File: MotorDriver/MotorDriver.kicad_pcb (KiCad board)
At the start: 2 copper layers, 109.9 x 40.6 mm, 66 parts, among them J1 Phase A, J10 PWR_D, J11 USART, J2 Phase B, J3 Phase C, J4 CAN, J5 IdSelect, J6 ST_LINK, J7 Hall, J8 Vbat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

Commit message: Finished printable parts
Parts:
- added C20: 10n, Capacitor_SMD:C_0603_1608Metric_Pad1.05x0.95mm_HandSolder, B.Cu at (134.6, 106.1)
- added C21: 10n, Capacitor_SMD:C_0603_1608Metric_Pad1.05x0.95mm_HandSolder, B.Cu at (134.6, 104.5)
- added C22: 10n, Capacitor_SMD:C_0603_1608Metric_Pad1.05x0.95mm_HandSolder, B.Cu at (134.6, 103.1)
- added C23: 100n, Capacitor_SMD:C_0603_1608Metric_Pad1.05x0.95mm_HandSolder, F.Cu at (133.1, 110.3)
- added D5: MRA4003T3G, Diode_SMD:D_SMA-SMB_Universal_Handsoldering, B.Cu at (125.9, 111.5)
- added R19: 100, Resistor_SMD:R_0603_1608Metric_Pad1.05x0.95mm_HandSolder, F.Cu at (131.9, 89.0)
- added R20: 100, Resistor_SMD:R_0603_1608Metric_Pad1.05x0.95mm_HandSolder, F.Cu at (131.9, 87.2)
- added R21: 3k3, Resistor_SMD:R_0603_1608Metric_Pad1.05x0.95mm_HandSolder, F.Cu at (138.2, 106.8)
- added R22: 3k3, Resistor_SMD:R_0603_1608Metric_Pad1.05x0.95mm_HandSolder, F.Cu at (140.7, 106.8)
- added R23: 3k3, Resistor_SMD:R_0603_1608Metric_Pad1.05x0.95mm_HandSolder, F.Cu at (143.3, 106.8)
- added R24: 2k2, Resistor_SMD:R_0603_1608Metric_Pad1.05x0.95mm_HandSolder, B.Cu at (138.2, 106.8)
- added R25: 2k2, Resistor_SMD:R_0603_1608Metric_Pad1.05x0.95mm_HandSolder, B.Cu at (140.7, 106.8)
- added R26: 2k2, Resistor_SMD:R_0603_1608Metric_Pad1.05x0.95mm_HandSolder, B.Cu at (143.3, 106.8)
- C16: moved to B.Cu
- D1: footprint Diode_SMD:D_SMA -> Diode_SMD:D_SMA-SMB_Universal_Handsoldering; moved to B.Cu
- moved D3 24.4 mm to (126.2, 107.4)
- moved C10 23.4 mm to (128.1, 108.5)
- moved C5 23.1 mm to (130.0, 108.5)
- moved R3 23.0 mm to (131.6, 108.5)
- moved D1 22.7 mm to (108.3, 107.5), turned to 90 degrees
- moved R14 22.7 mm to (121.7, 108.1)
- moved C16 21.7 mm to (134.6, 101.5)
- moved J2 21.3 mm to (196.1, 94.2)
- moved J5 21.3 mm to (137.0, 94.6)
- moved Q3 21.3 mm to (182.0, 94.2)
- moved C1 21.3 mm to (108.5, 102.6)
- moved H1 21.3 mm to (202.4, 109.5)
- moved H2 21.3 mm to (202.4, 79.0)
- moved J1 21.3 mm to (196.1, 103.8)
- moved J3 21.3 mm to (196.1, 84.7)
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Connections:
- J11 pad 2: /procesorová jednotka/USART_TX -> Net-(J11-Pad2)
- J11 pad 3: /procesorová jednotka/USART_RX -> Net-(J11-Pad3)
- J7 pad 2: /procesorová jednotka/HAL_C -> Net-(J7-Pad2)
- J7 pad 3: /procesorová jednotka/HAL_B -> Net-(J7-Pad3)
- J7 pad 4: /procesorová jednotka/HAL_A -> Net-(J7-Pad4)
- J7 pad 5: +5V -> Net-(C23-Pad1)
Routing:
- net GNDS: track 220.7 -> 163.1 mm, vias 20 -> 19
- net +3V3: track 82.9 -> 106.8 mm, vias 5 -> 7
- net +5V: track 55.3 -> 41.3 mm, vias 0 -> 1
- net Net-(J11-Pad2): track 0.00 -> 12.2 mm
- net /procesorová jednotka/USART_TX: track 16.0 -> 5.02 mm
- net +9V: track 15.6 -> 8.99 mm
- net Net-(C23-Pad1): track 0.00 -> 6.50 mm, vias 0 -> 1
- net Net-(J11-Pad3): track 0.00 -> 5.64 mm
- net Net-(J7-Pad4): track 0.00 -> 5.08 mm
- net Net-(J7-Pad3): track 0.00 -> 5.08 mm
- net Net-(J7-Pad2): track 0.00 -> 5.08 mm
- net /procesorová jednotka/USART_RX: track 11.8 -> 7.29 mm
- net /power/pwrs_in: track 6.23 -> 9.10 mm, vias 0 -> 1
- net /procesorová jednotka/HAL_A: track 23.3 -> 21.7 mm, vias 0 -> 1
- net /procesorová jednotka/CONF_2: track 12.3 -> 13.7 mm
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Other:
- net class PWR: clearance 0.5 -> 0.2
- net class PWRS: clearance 0.3 -> 0.2
- net class PWRS_IN: clearance 0.3 -> 0.2
- board text added: "A"
- board text added: "B"
- board text added: "C"
- board text added: "Hall"
- board text added: "Murphy II Motor driver rev. 1.0"
- board text added: "PhA"
- board text added: "PhB"
- board text added: "PhC"
- board text removed: "HA"
- board text removed: "HB"
- board text removed: "HC"

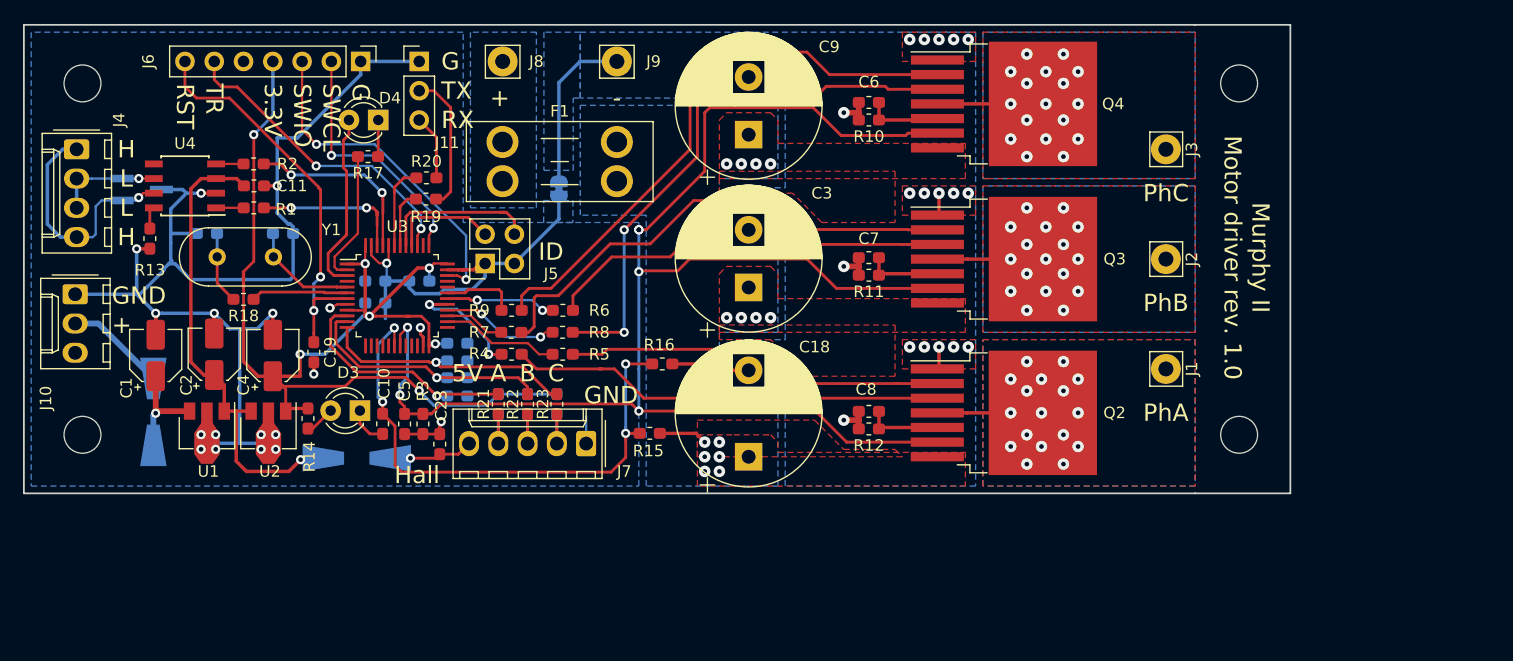
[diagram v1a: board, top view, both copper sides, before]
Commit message: Power and output ping changed roblaced by holes. Correction of tracks width and vias diameters.
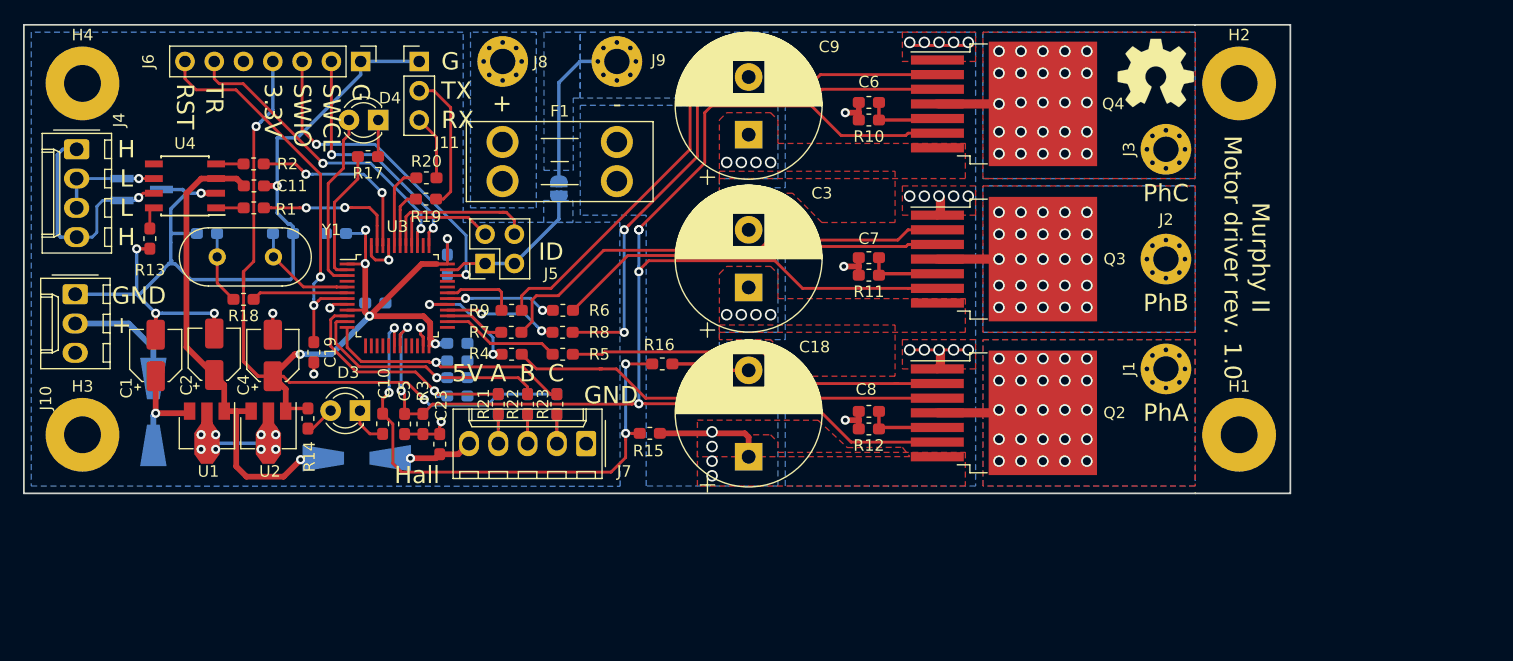
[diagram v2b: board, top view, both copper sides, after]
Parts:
- added REF**: OSHW-Symbol_6.7x6mm_SilkScreen, Symbol:OSHW-Symbol_6.7x6mm_SilkScreen, F.Cu at (195.2, 78.1)
- H1, H2, H3, H4: value MountingHole -> MountingHole_Pad; footprint MountingHole:MountingHole_3.2mm_M3_ISO7380 -> MountingHole:MountingHole_3.2mm_M3_Pad
- J1, J2, J3, J9: footprint Connector_Pin:Pin_D1.4mm_L8.5mm_W2.8mm_FlatFork -> MountingHole:MountingHole_2.2mm_M2_Pad_Via
- J8: value Vbat -> BAT+; footprint Connector_Pin:Pin_D1.4mm_L8.5mm_W2.8mm_FlatFork -> MountingHole:MountingHole_2.2mm_M2_Pad_Via
- JP1: footprint Jumper:SolderJumper-2_P1.3mm_Bridged_RoundedPad1.0x1.5mm -> Jumper:SolderJumper-2_P1.3mm_Open_RoundedPad1.0x1.5mm
- moved C15 5.36 mm to (124.1, 92.0), turned to 180 degrees
- moved C14 2.82 mm to (133.8, 94.7), turned to 270 degrees
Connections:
- H1 pad 1: (no net) -> Net-(H1-Pad1)
- H2 pad 1: (no net) -> Net-(H2-Pad1)
- H3 pad 1: (no net) -> GNDS
- H4 pad 1: (no net) -> GNDS
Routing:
- net GNDS: track 163.1 -> 127.6 mm
- net GNDPWR: track 34.1 -> 46.5 mm
- net +36V: track 4.20 -> 9.54 mm, vias 14 -> 12
- net /H můstky/OUT_C: track 6.36 -> 10.2 mm, vias 17 -> 25
- net /H můstky/OUT_B: track 9.15 -> 13.0 mm, vias 17 -> 25
- net Net-(Q4-Pad2): track 50.6 -> 47.6 mm
- net /H můstky/OUT_A: track 6.37 -> 9.15 mm, vias 17 -> 25
- net Net-(Q3-Pad2): track 43.3 -> 40.9 mm
- net Net-(C23-Pad1): track 6.50 -> 8.26 mm
- net +3V3: track 106.8 -> 108.4 mm, vias 7 -> 8
- net +9V: track 8.99 -> 10.5 mm
- net /interface/CANtx: track 14.1 -> 12.7 mm
- net /power/PWR_SENSE: track 49.5 -> 48.3 mm
- net /H můstky/I_SENSE: track 135.3 -> 134.2 mm
- net /H můstky/INH_A: track 11.4 -> 10.4 mm
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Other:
- net class PWR: via_dia 1 -> 0.8
- rule trace_min: 0.2 -> 0.25

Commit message: Added filter capacitors to low votlage power supply
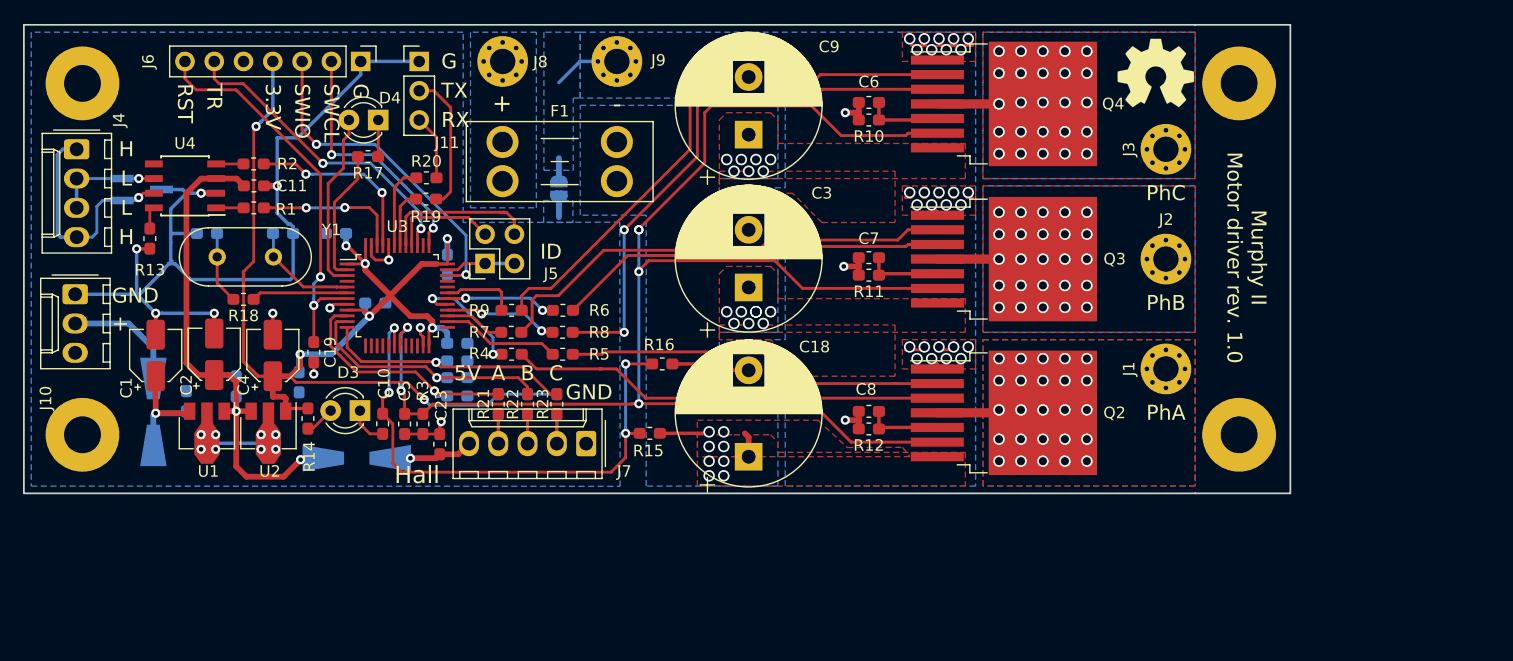
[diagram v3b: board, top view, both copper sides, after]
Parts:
- added C24: 100nF, Capacitor_SMD:C_0603_1608Metric_Pad1.05x0.95mm_HandSolder, B.Cu at (111.1, 106.6)
- added C25: 100nF, Capacitor_SMD:C_0603_1608Metric_Pad1.05x0.95mm_HandSolder, B.Cu at (115.4, 105.3)
- added C26: 100nF, Capacitor_SMD:C_0603_1608Metric_Pad1.05x0.95mm_HandSolder, B.Cu at (120.9, 104.9)
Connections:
- H1 pad 1: Net-(H1-Pad1) -> (no net)
- H2 pad 1: Net-(H2-Pad1) -> (no net)
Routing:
- net GNDPWR: track 46.5 -> 35.6 mm, vias 18 -> 30
- net GNDS: track 127.6 -> 122.0 mm
- net +5V: track 41.7 -> 45.3 mm, vias 1 -> 2
- net +36V: track 9.54 -> 6.49 mm, vias 12 -> 24
- net /power/pwrs_in: track 9.10 -> 11.8 mm
